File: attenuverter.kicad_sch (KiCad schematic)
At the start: 42 parts, among them U301 OPA4991, U302 TL072

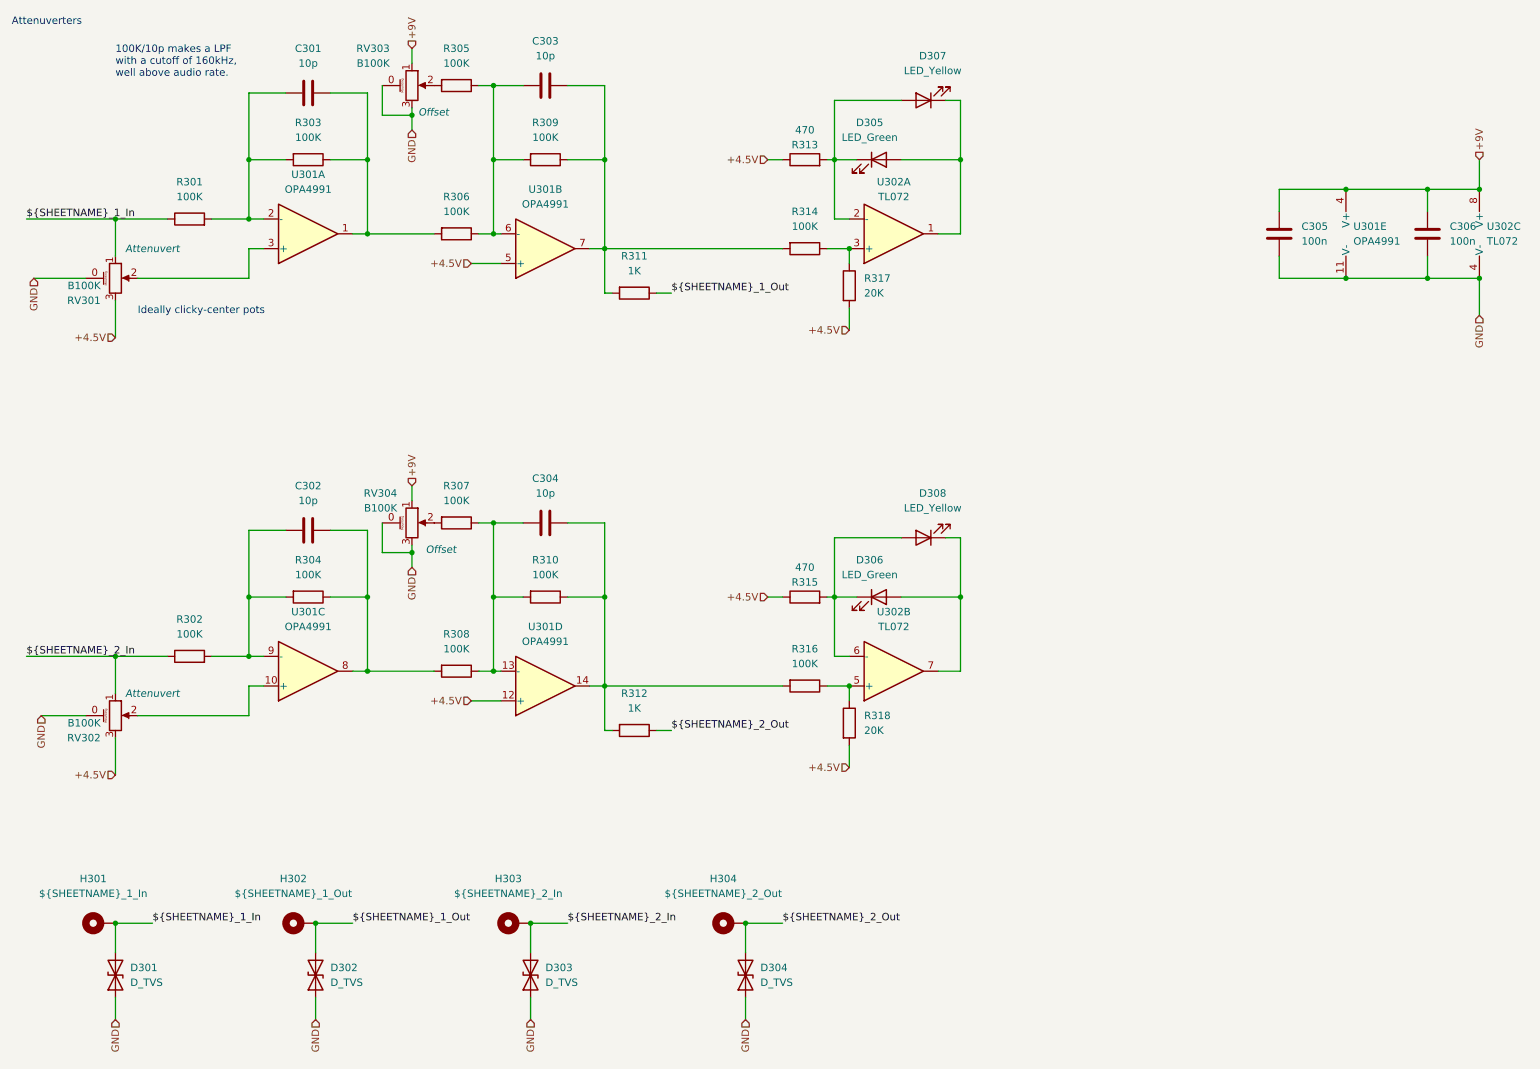
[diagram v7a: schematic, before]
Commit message: Update attenuverter labels to get rid of warnings
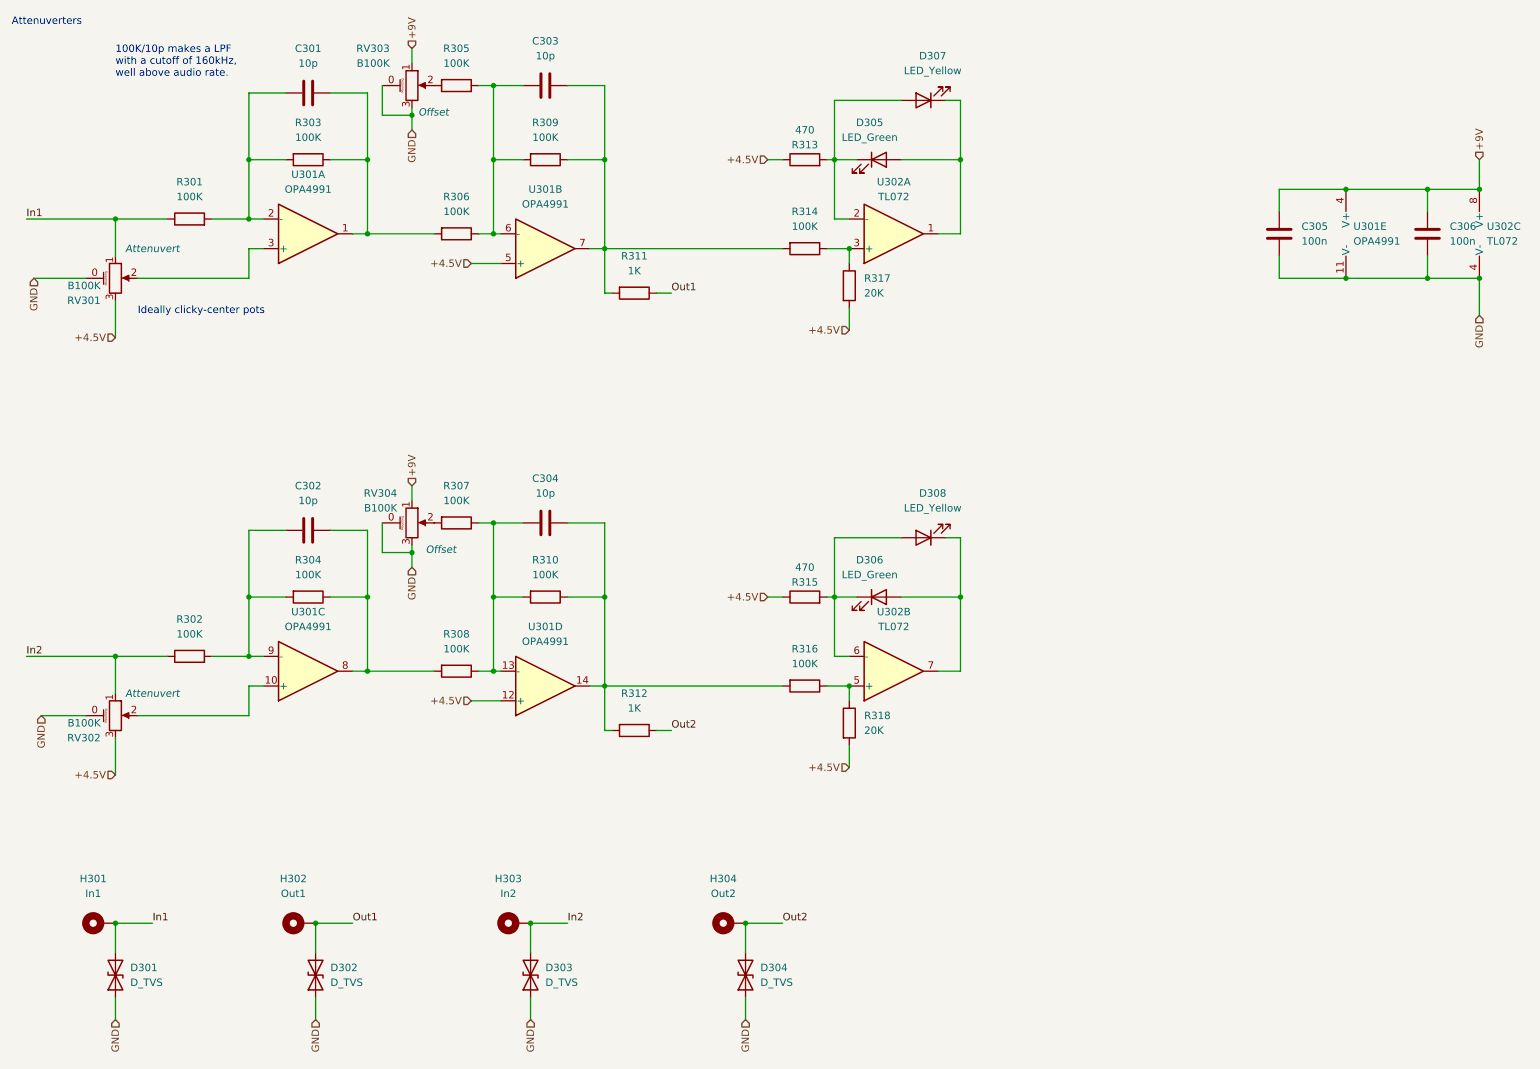
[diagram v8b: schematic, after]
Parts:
- H301: value ${SHEETNAME}_1_In -> In1
- H302: value ${SHEETNAME}_1_Out -> Out1
- H303: value ${SHEETNAME}_2_In -> In2
- H304: value ${SHEETNAME}_2_Out -> Out2
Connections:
- net ${SHEETNAME}_1_In renamed In1
- net ${SHEETNAME}_1_Out renamed Out1
- net ${SHEETNAME}_2_In renamed In2
- net ${SHEETNAME}_2_Out renamed Out2
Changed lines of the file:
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@@
     (effects (font (size 1.27 1.27)) (justify left bottom))
   )
-  (label "${SHEETNAME}_2_Out" (at 147.32 170.18 0)
-    (effects (font (size 1.27 1.27)) (justify left bottom))
-  )
-  (label "${SHEETNAME}_1_Out" (at 73.66 170.18 0)
-    (effects (font (size 1.27 1.27)) (justify left bottom))
-  )
-  (label "${SHEETNAME}_2_In" (at 17.78 124.46 0)
-    (effects (font (size 1.27 1.27)) (justify left bottom))
-  )
-  (label "${SHEETNAME}_2_Out" (at 128.27 137.16 0)
-    (effects (font (size 1.27 1.27)) (justify left bottom))
-  )
-  (label "${SHEETNAME}_2_In" (at 110.49 170.18 0)
-    (effects (font (size 1.27 1.27)) (justify left bottom))
-  )
-  (label "${SHEETNAME}_1_In" (at 17.78 49.53 0)
-    (effects (font (size 1.27 1.27)) (justify left bottom))
-  )
-  (label "${SHEETNAME}_1_In" (at 39.37 170.18 0)
-    (effects (font (size 1.27 1.27)) (justify left bottom))
-  )
-  (label "${SHEETNAME}_1_Out" (at 128.27 62.23 0)
+  (label "Out2" (at 147.32 170.18 0)
+    (effects (font (size 1.27 1.27)) (justify left bottom))
+  )
+  (label "Out1" (at 73.66 170.18 0)
+    (effects (font (size 1.27 1.27)) (justify left bottom))
+  )
+  (label "In2" (at 17.78 124.46 0)
+    (effects (font (size 1.27 1.27)) (justify left bottom))
+  )
+  (label "Out2" (at 128.27 137.16 0)
+    (effects (font (size 1.27 1.27)) (justify left bottom))
+  )
+  (label "In2" (at 110.49 170.18 0)
+    (effects (font (size 1.27 1.27)) (justify left bottom))
+  )
+  (label "In1" (at 17.78 49.53 0)
+    (effects (font (size 1.27 1.27)) (justify left bottom))
+  )
+  (label "In1" (at 39.37 170.18 0)
+    (effects (font (size 1.27 1.27)) (justify left bottom))
+  )
+  (label "Out1" (at 128.27 62.23 0)
     (effects (font (size 1.27 1.27)) (justify left bottom))
   )
@@
     (in_bom yes) (on_board yes) (fields_autoplaced)
     (property "Reference" "H301" (id 0) (at 29.21 162.56 90))
-    (property "Value" "${SHEETNAME}_1_In" (id 1) (at 29.21 165.1 90))
+    (property "Value" "In1" (id 1) (at 29.21 165.1 90))
     (property "Footprint" "MountingHole:MountingHole_4.3mm_M4_Pad_TopBottom" (id 2) (at 30.48 170.18 0)
       (effects (font (size 1.27 1.27)) hide)
@@
     (in_bom yes) (on_board yes) (fields_autoplaced)
     (property "Reference" "H304" (id 0) (at 137.16 162.56 90))
-    (property "Value" "${SHEETNAME}_2_Out" (id 1) (at 137.16 165.1 90))
+    (property "Value" "Out2" (id 1) (at 137.16 165.1 90))
     (property "Footprint" "MountingHole:MountingHole_4.3mm_M4_Pad_TopBottom" (id 2) (at 138.43 170.18 0)
       (effects (font (size 1.27 1.27)) hide)
@@
     (in_bom yes) (on_board yes) (fields_autoplaced)
     (property "Reference" "H303" (id 0) (at 100.33 162.56 90))
-    (property "Value" "${SHEETNAME}_2_In" (id 1) (at 100.33 165.1 90))
+    (property "Value" "In2" (id 1) (at 100.33 165.1 90))
     (property "Footprint" "MountingHole:MountingHole_4.3mm_M4_Pad_TopBottom" (id 2) (at 101.6 170.18 0)
       (effects (font (size 1.27 1.27)) hide)
@@
     (in_bom yes) (on_board yes) (fields_autoplaced)
     (property "Reference" "H302" (id 0) (at 63.5 162.56 90))
-    (property "Value" "${SHEETNAME}_1_Out" (id 1) (at 63.5 165.1 90))
+    (property "Value" "Out1" (id 1) (at 63.5 165.1 90))
     (property "Footprint" "MountingHole:MountingHole_4.3mm_M4_Pad_TopBottom" (id 2) (at 64.77 170.18 0)
       (effects (font (size 1.27 1.27)) hide)
